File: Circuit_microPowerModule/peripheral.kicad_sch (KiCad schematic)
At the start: 3 parts, among them J2 Jack-DC, J3 Screw_Terminal_01x02

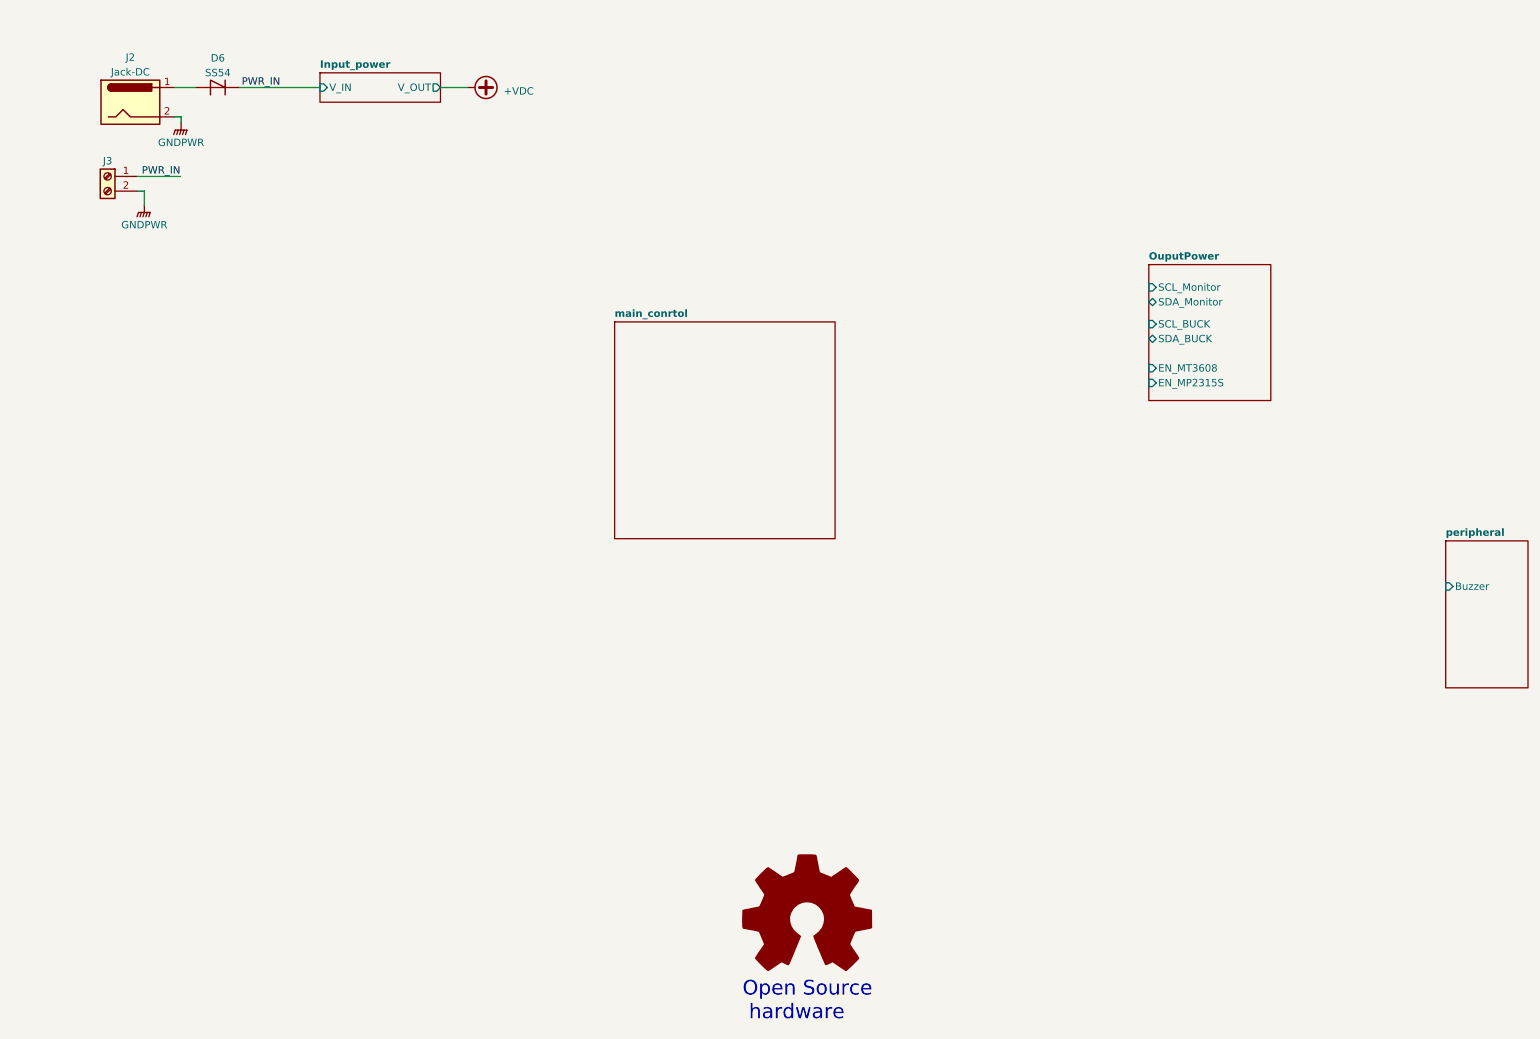
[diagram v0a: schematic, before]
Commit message: added boost circuit
create peripheral schematic
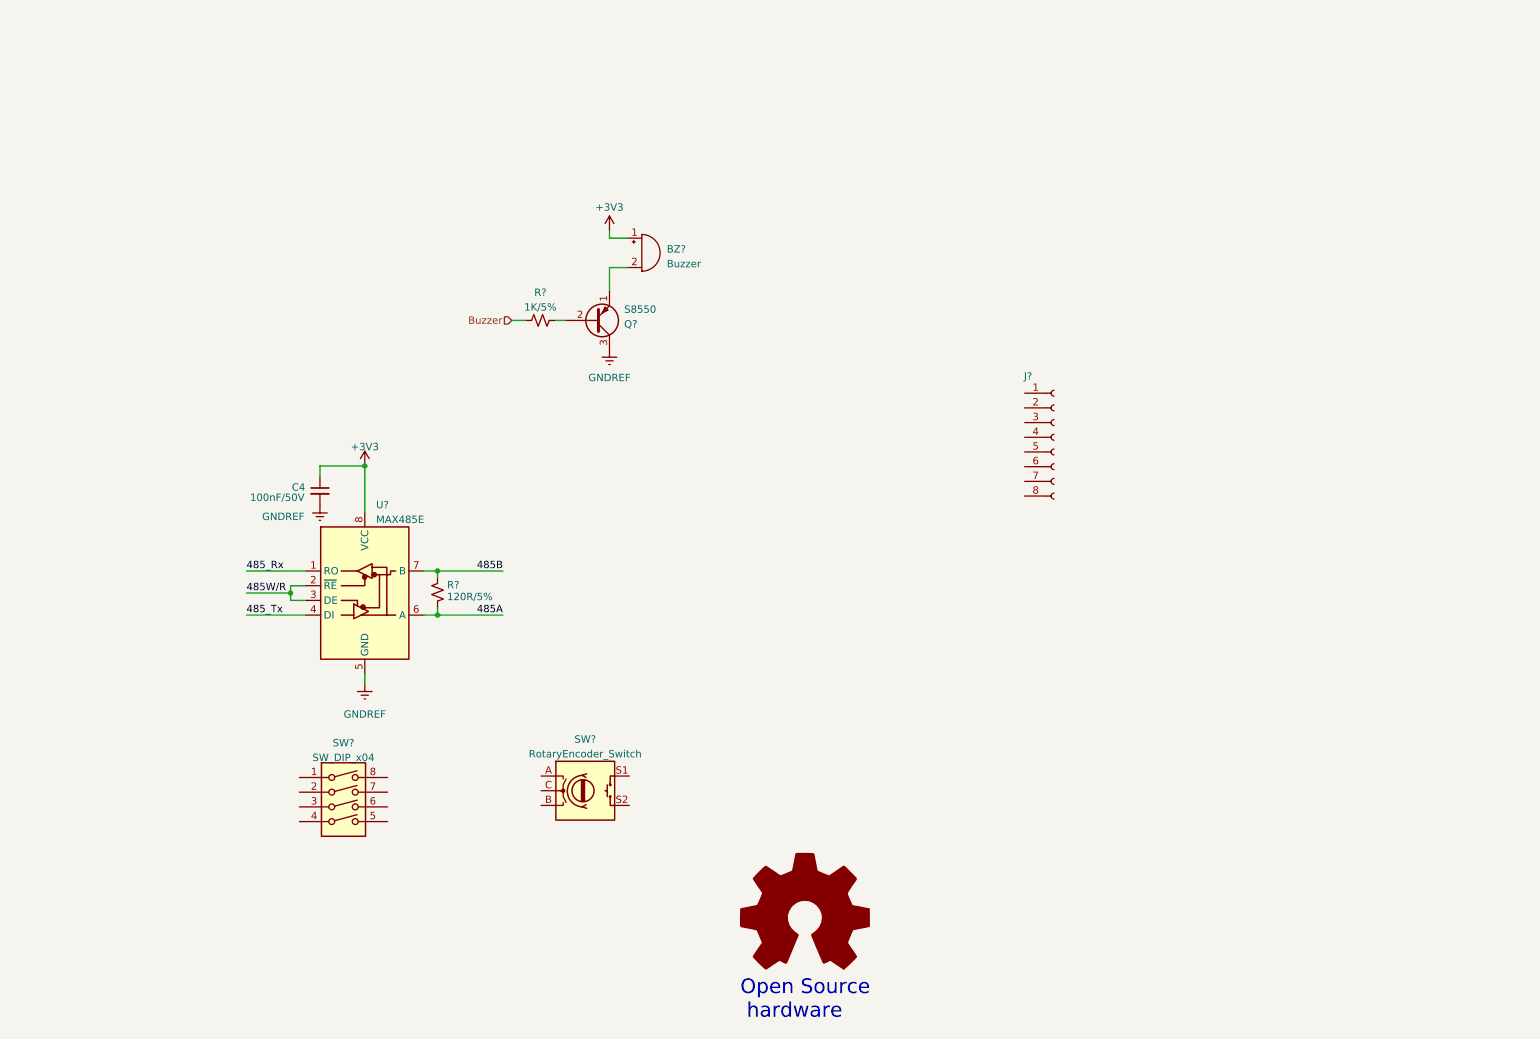
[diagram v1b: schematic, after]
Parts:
- removed D6: SS54, symbol Device:D_Shockley
- removed J2: Jack-DC, symbol Connector:Jack-DC
- removed J3: Screw_Terminal_01x02, symbol Connector:Screw_Terminal_01x02
- added BZ?: Buzzer, symbol Device:Buzzer
- added C4: 100nF/50V, symbol Device:C_Small
- added J?: Conn_01x08_Socket, symbol Connector:Conn_01x08_Socket
- added Q?: S8550, Package_TO_SOT_THT:TO-92_Inline, symbol Transistor_BJT:S8550
- added R?: 120R/5%, Resistor_SMD:R_0603_1608Metric, symbol Device:R_Small_US
- added R?: 1K/5%, Resistor_SMD:R_0603_1608Metric, symbol Device:R_Small_US
- added SW?: RotaryEncoder_Switch, symbol Device:RotaryEncoder_Switch
- added SW?: SW_DIP_x04, symbol Switch:SW_DIP_x04
- added U?: MAX485E, symbol Interface_UART:MAX485E
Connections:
- new net: BZ?.2 (+), Q?.1 (E)
- new net: Q?.2 (B), R?.2
- new net +3V3: BZ?.1 (-), C4.1, U?.8 (VCC)
- new net 485A: R?.2, U?.6 (A)
- new net 485B: R?.1, U?.7 (B)
- new net 485W/R: U?.2 (~{RE}), U?.3 (DE)
- new net 485_Rx: U?.1 (RO)
- new net 485_Tx: U?.4 (DI)
- new net Buzzer: R?.1
- new net GNDREF: C4.2, Q?.3 (C), U?.5 (GND)
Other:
- removed sheet Input_power
- removed sheet OuputPower
- removed sheet main_conrtol
- removed sheet peripheral
- title: µPower Module -> (none)

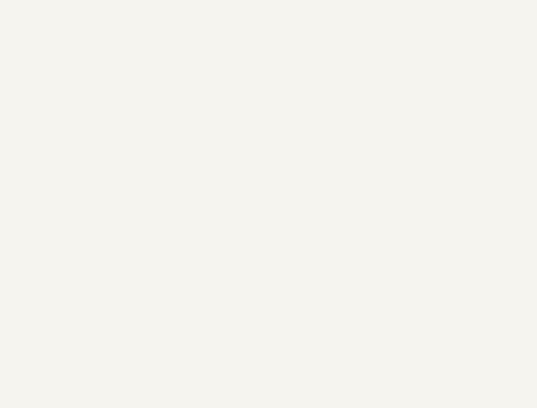
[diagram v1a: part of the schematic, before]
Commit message: added mikrobus header
added filter capacitance, I2C pull-up resistor
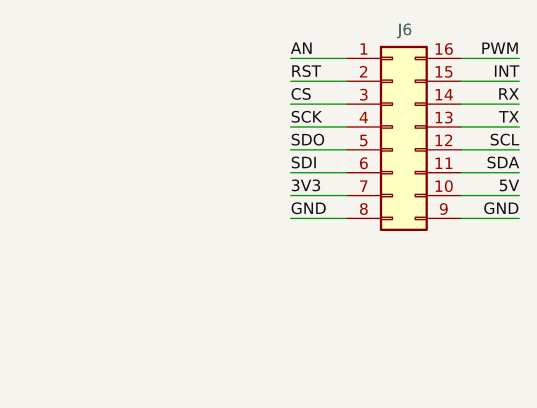
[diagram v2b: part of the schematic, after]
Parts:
- added J6: MikroBus, symbol Connector_Generic:Conn_02x08_Counter_Clockwise
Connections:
- new net 3V3: J6.7 (Pin_7)
- new net 5V: J6.10 (Pin_10)
- new net AN: J6.1 (Pin_1)
- new net CS: J6.3 (Pin_3)
- new net GND: J6.8 (Pin_8), J6.9 (Pin_9)
- new net INT: J6.15 (Pin_15)
- new net PWM: J6.16 (Pin_16)
- new net RST: J6.2 (Pin_2)
- new net RX: J6.14 (Pin_14)
- new net SCK: J6.4 (Pin_4)
- new net SCL: J6.12 (Pin_12)
- new net SDA: J6.11 (Pin_11)
- new net SDI: J6.6 (Pin_6)
- new net SDO: J6.5 (Pin_5)
- new net TX: J6.13 (Pin_13)

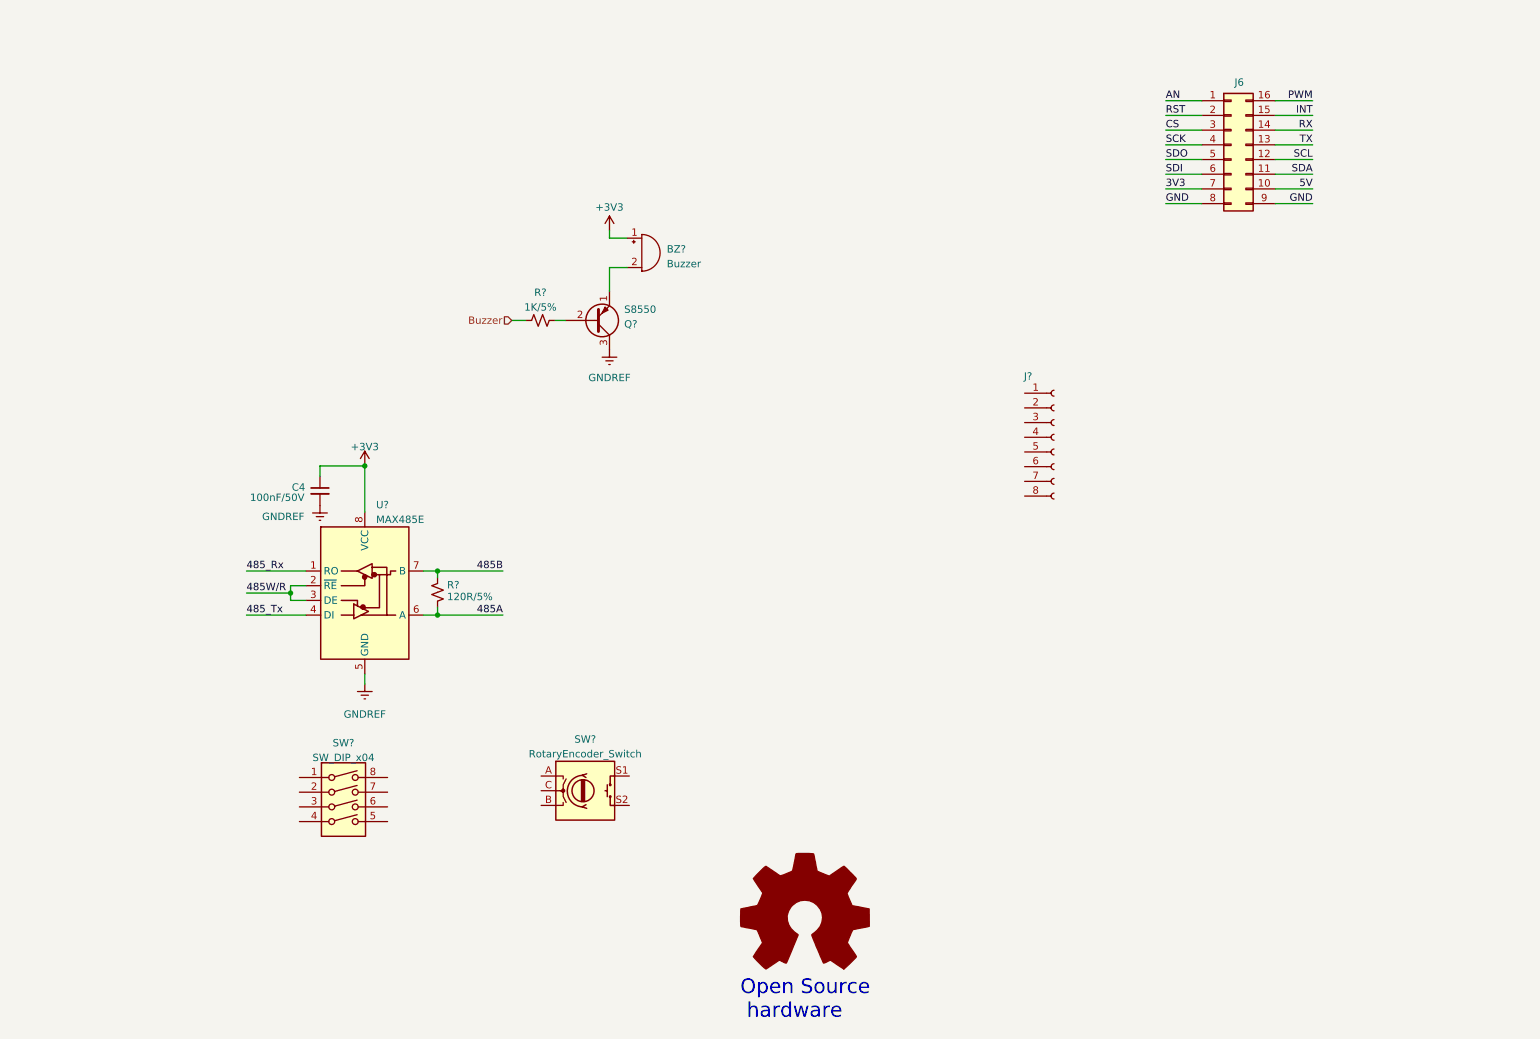
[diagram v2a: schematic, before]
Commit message: added Nokia 5110 LCD symbol
linked some component pin
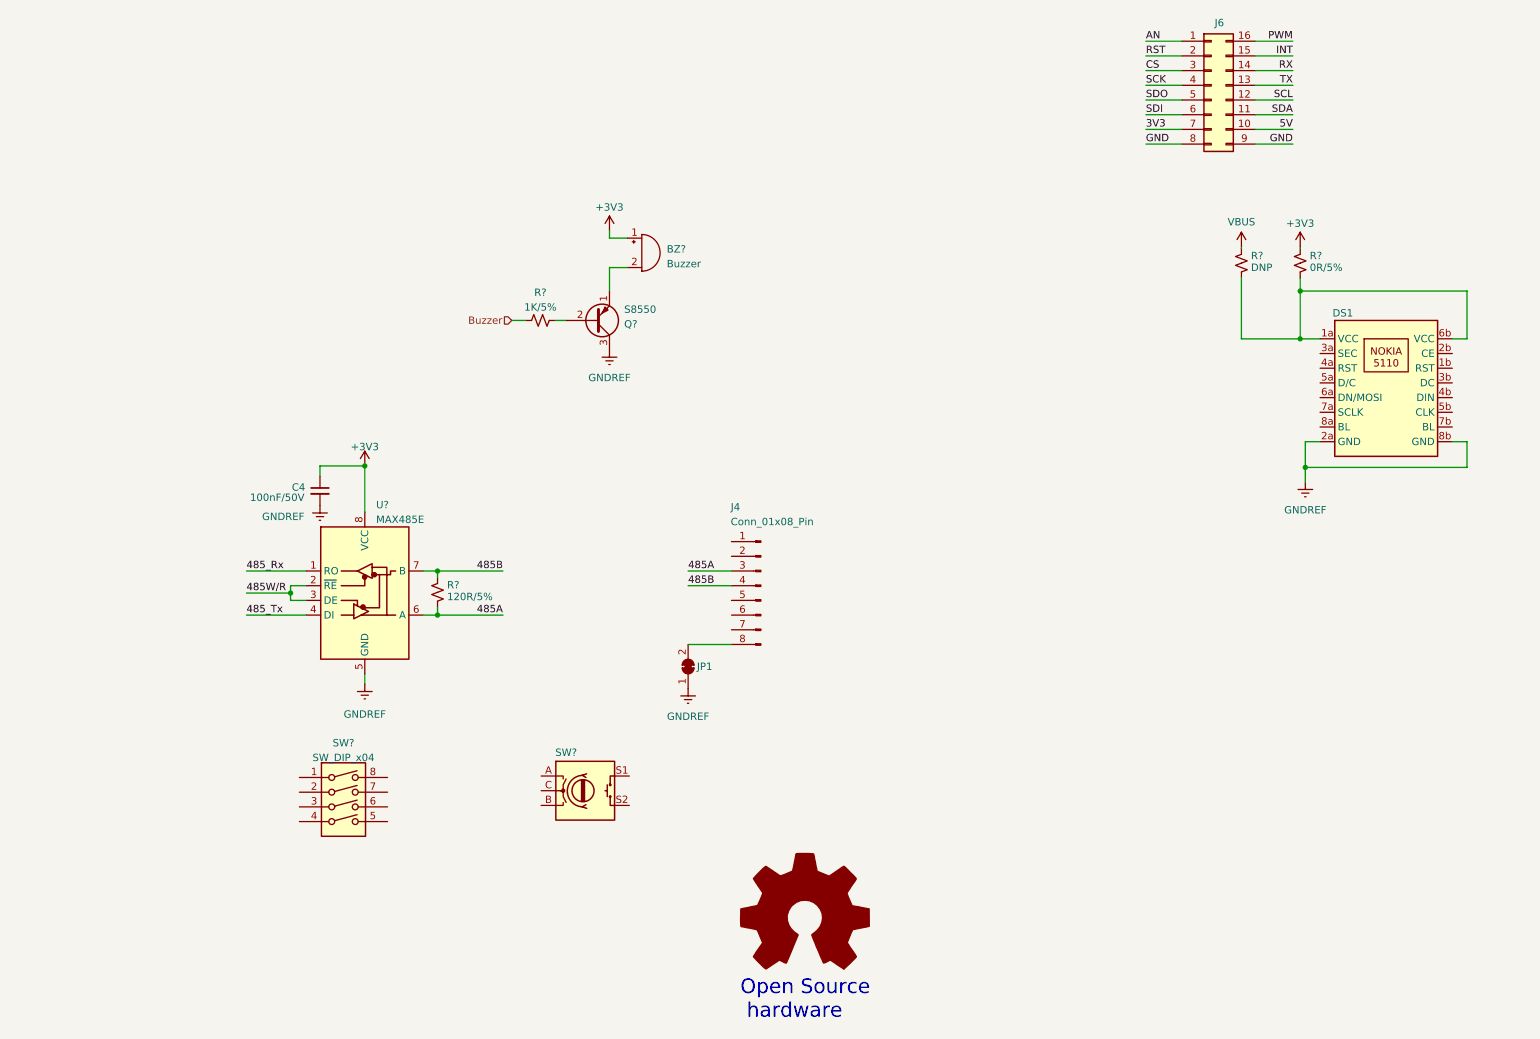
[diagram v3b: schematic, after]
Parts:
- removed J?: Conn_01x08_Socket, symbol Connector:Conn_01x08_Socket
- added DS1: ~, symbol micro-PowerModule:PCD8544
- added J4: Conn_01x08_Pin, symbol Connector:Conn_01x08_Pin
- added JP1: SolderJumper_2_Bridged, Jumper:SolderJumper-2_P1.3mm_Bridged_Pad1.0x1.5mm, symbol Jumper:SolderJumper_2_Bridged
- added R?: 0R/5%, Resistor_SMD:R_0603_1608Metric, symbol Device:R_Small_US
- added R?: DNP, Resistor_SMD:R_0603_1608Metric, symbol Device:R_Small_US
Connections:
- net +3V3: now also R?.1
- net 485A: now also J4.3 (Pin_3)
- net 485B: now also J4.4 (Pin_4)
- net GNDREF: now also DS1.2a (GND), DS1.8b (GND), JP1.1 (A)
- new net: DS1.1a (VCC), DS1.6b (VCC), R?.2, R?.2
- new net: J4.8 (Pin_8), JP1.2 (B)
- new net VBUS: R?.1
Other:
- moved on the sheet: J6

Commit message: added schematic svg file
added encoder wire, mikrobus connect
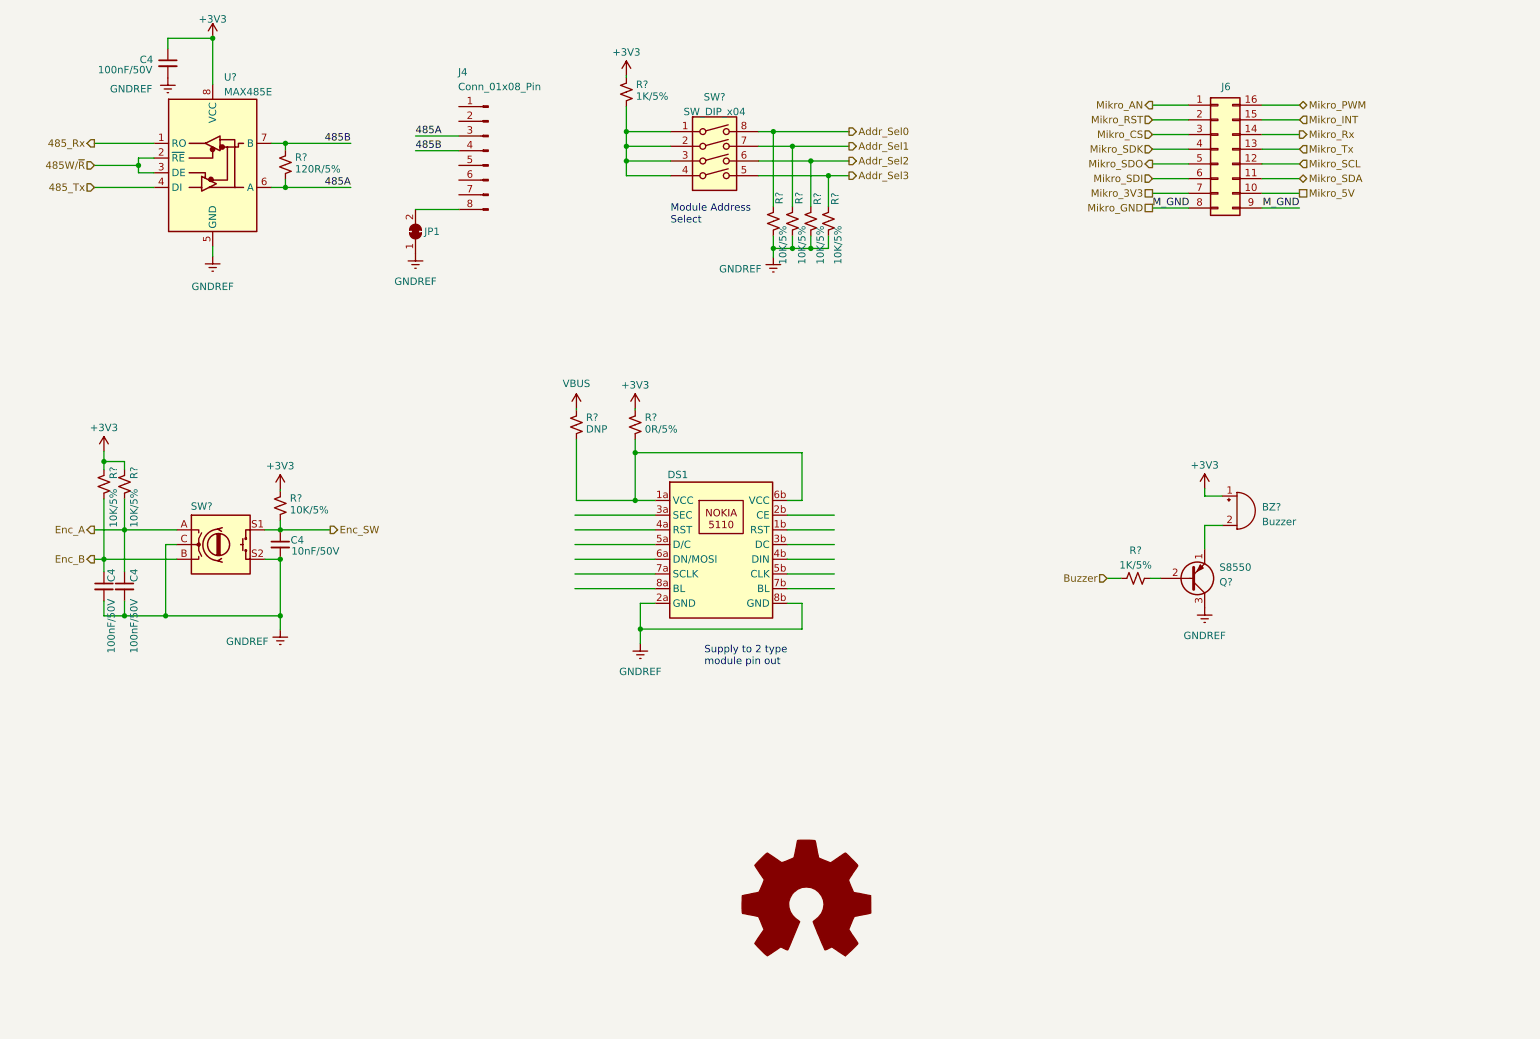
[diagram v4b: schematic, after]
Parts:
- added C4 (x2): 100nF/50V, symbol Device:C_Small
- added C4: 10nF/50V, symbol Device:C_Small
- added R? (x7): 10K/5%, Resistor_SMD:R_0603_1608Metric, symbol Device:R_Small_US
- added R?: 1K/5%, Resistor_SMD:R_0603_1608Metric, symbol Device:R_Small_US
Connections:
- net +3V3: now also R?.1, R?.1, R?.1, R?.1
- net GNDREF: now also SW?.C, SW?.S2, C4.2, C4.2, C4.2, R?.2, R?.2, R?.2, R?.2
- net Enc_A: now reaches SW?.A
- net Enc_A: now also C4.1, R?.2
- net Enc_B: now reaches SW?.B
- net Enc_B: now also C4.1, R?.2
- net Enc_SW: now reaches SW?.S1
- net Enc_SW: now also C4.1, R?.2
- net at SW?.1: now also SW?.2, SW?.3, SW?.4, R?.2
- net Addr_Sel3: now reaches SW?.5
- net Addr_Sel3: now also R?.1
- net Addr_Sel2: now reaches SW?.6
- net Addr_Sel2: now also R?.1
- net Addr_Sel1: now reaches SW?.7
- net Addr_Sel1: now also R?.1
- net Addr_Sel0: now reaches SW?.8
- net Addr_Sel0: now also R?.1
- net 3V3 renamed Mikro_3V3
- net 485W/R renamed 485W/~{R}
- net 5V renamed Mikro_5V
- net AN renamed Mikro_AN
- net CS renamed Mikro_CS
- net GND renamed Mikro_GND
- net INT renamed Mikro_INT
- net PWM renamed Mikro_PWM
- net RST renamed Mikro_RST
- net RX renamed Mikro_Rx
- net SCK renamed Mikro_SDK
- net SCL renamed Mikro_SCL
- net SDA renamed Mikro_SDA
- net SDI renamed Mikro_SDI
- net SDO renamed Mikro_SDO
- net TX renamed Mikro_Tx
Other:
- note removed: "Open Source hardware"
- moved on the sheet: BZ?, C4, DS1, J4, J6, JP1, Q?, R?, SW?, U?
